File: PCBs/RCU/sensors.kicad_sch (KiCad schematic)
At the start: 4 parts

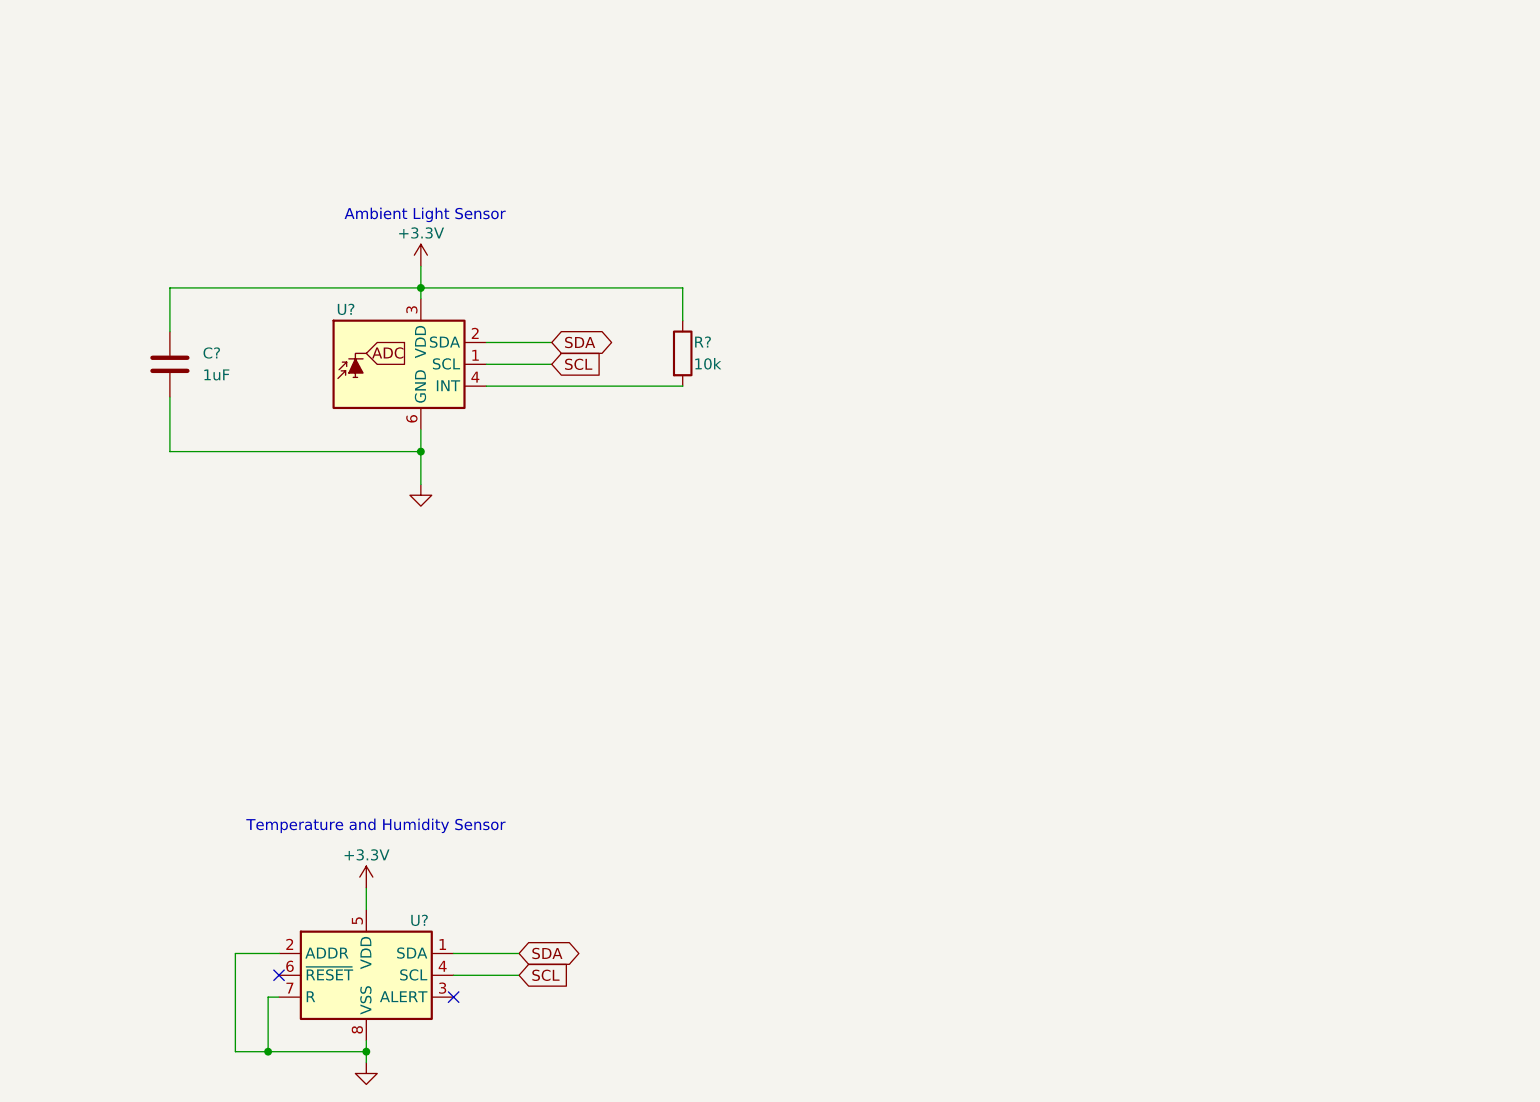
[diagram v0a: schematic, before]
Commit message: Added Accelerometer_Gyroscope IC with supplementary components
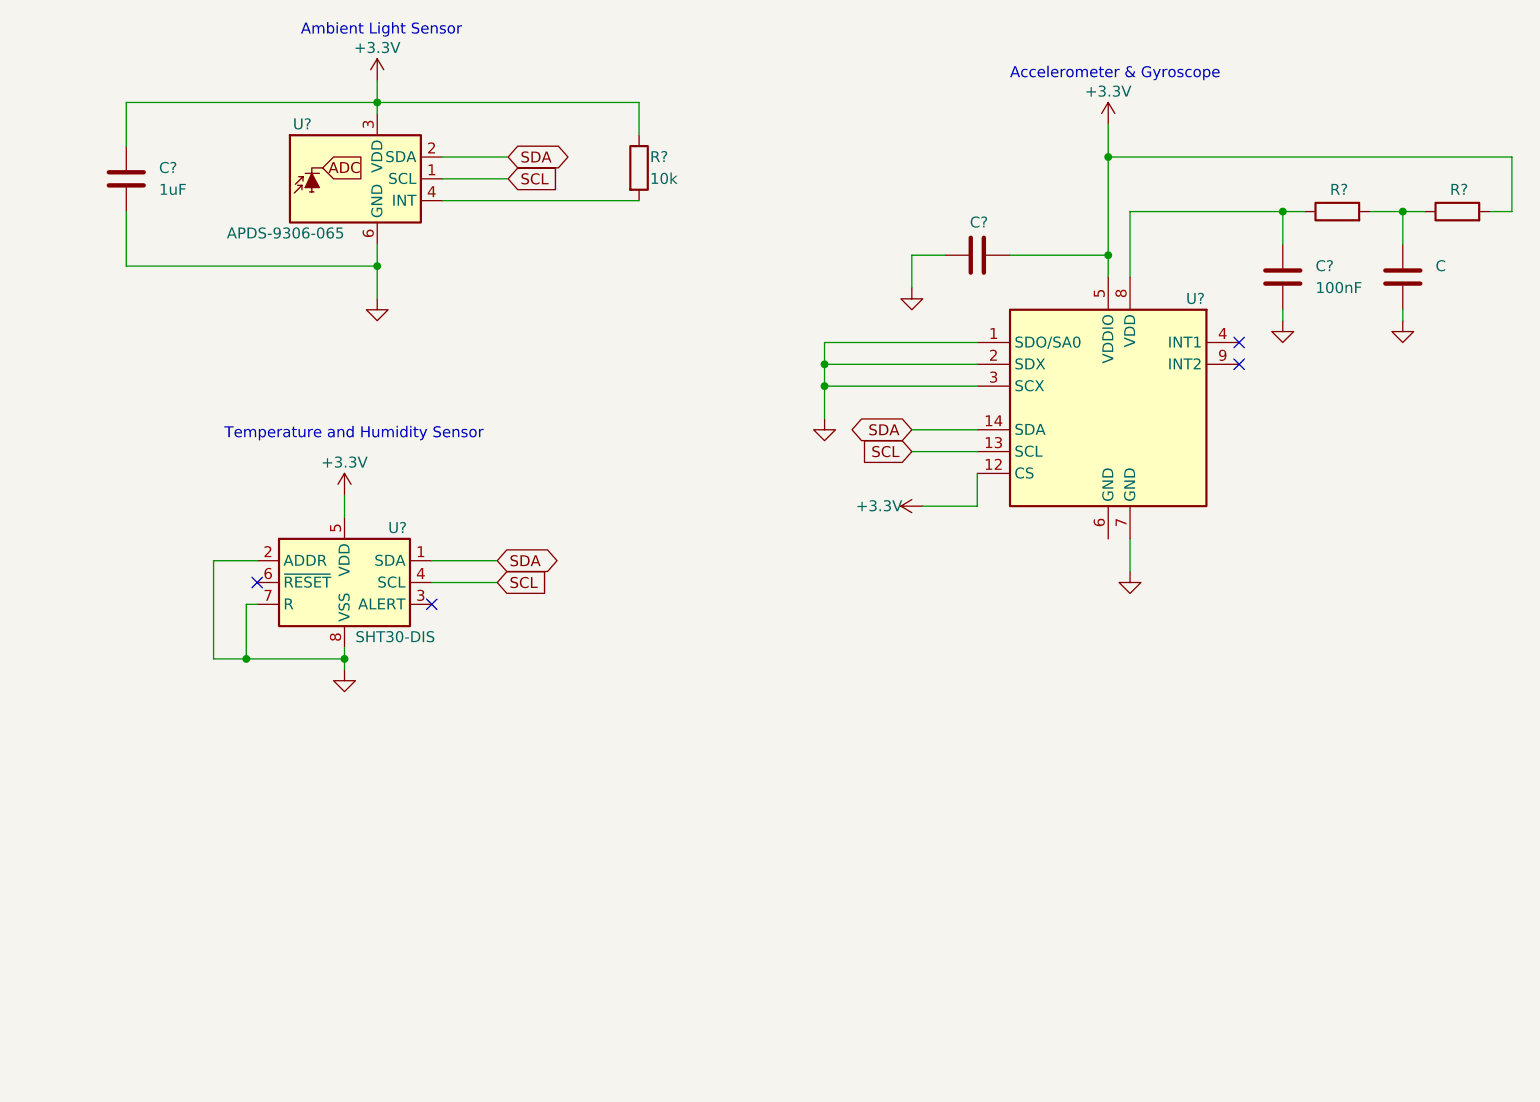
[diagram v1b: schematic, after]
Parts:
- added C, C?: (no value), symbol Device:C
- added C?: 100nF, symbol Device:C
- added R? (x2): (no value), symbol Device:R
- added U?: (no value), symbol Sensor_Motion:LSM6DS3
- U?: value (none) -> SHT30-DIS; footprint (none) -> Sensor_Humidity:Sensirion_DFN-8-1EP_2.5x2.5mm_P0.5mm_EP1.1x1.7mm
- U?: value (none) -> APDS-9306-065; footprint (none) -> OptoDevice:Broadcom_DFN-6_2x2mm_P0.65mm
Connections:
- net +3V3: now also C?.2, R?.2, U?.12 (CS), U?.5 (VDDIO)
- net GND: now also C.1, C?.1, C?.1, U?.1 (SDO/SA0), U?.2 (SDX), U?.3 (SCX), U?.7 (GND)
- net SCL: now also U?.13 (SCL)
- net SDA: now also U?.14 (SDA)
- new net: C?.2, R?.1, U?.8 (VDD)
- new net: C.2, R?.1, R?.2
- no-connect marks 2 -> 4
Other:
- note added: "Accelerometer & Gyroscope"
- moved on the sheet: C?, R?, U?

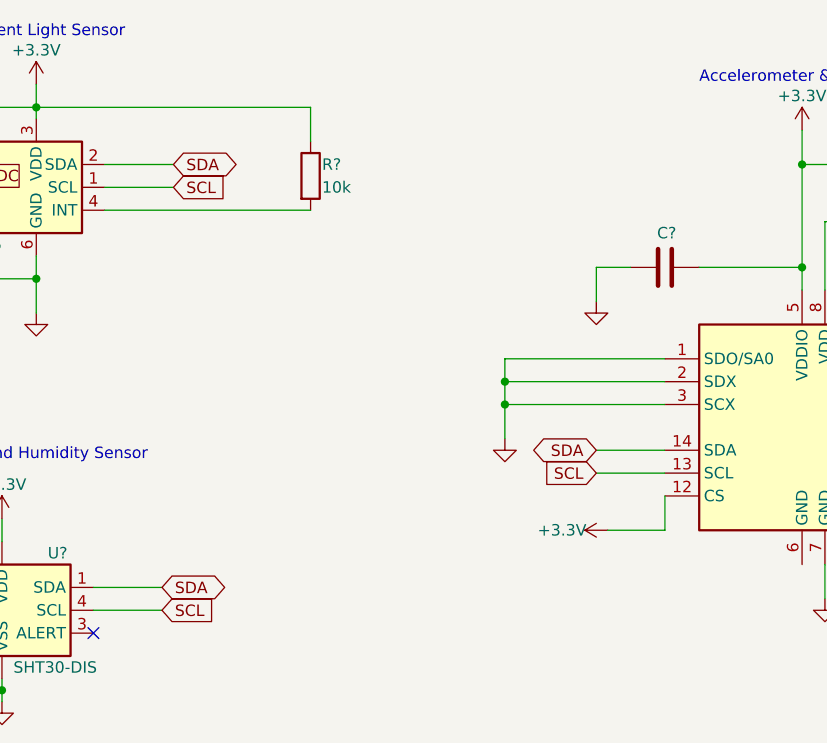
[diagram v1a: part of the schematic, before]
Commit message: Prepended 'SDA' and 'SCL' global labels with 'I2C_'
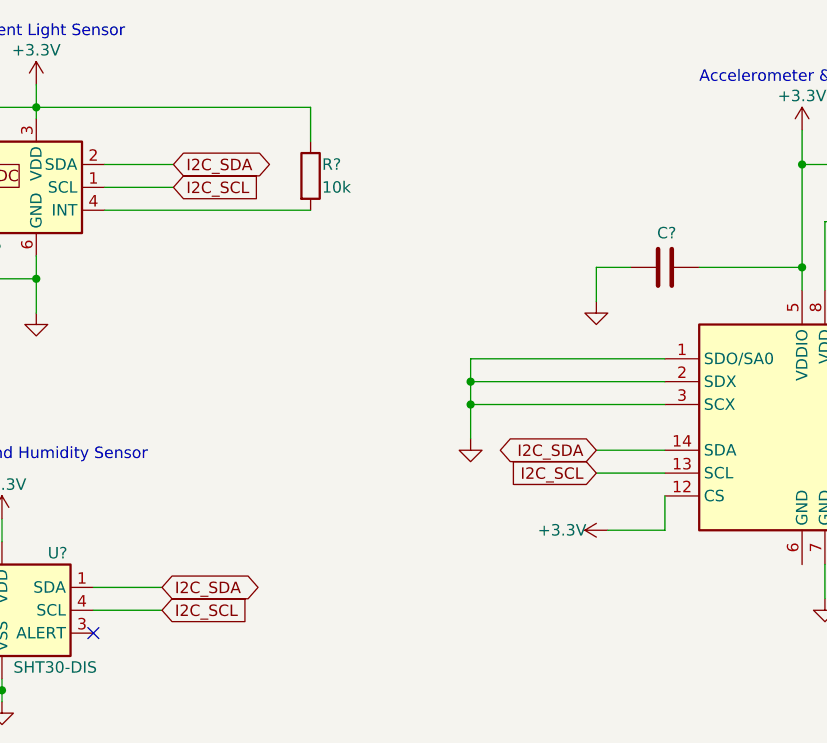
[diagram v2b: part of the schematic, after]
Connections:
- net SCL renamed I2C_SCL
- net SDA renamed I2C_SDA
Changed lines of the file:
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@@
   (junction (at 161.29 40.64) (diameter 0) (color 0 0 0 0)
   )
-  (junction (at 107.95 58.42) (diameter 0) (color 0 0 0 0)
+  (junction (at 104.14 58.42) (diameter 0) (color 0 0 0 0)
   )
   (junction (at 40.64 92.71) (diameter 0) (color 0 0 0 0)
   )
-  (junction (at 107.95 60.96) (diameter 0) (color 0 0 0 0)
+  (junction (at 104.14 60.96) (diameter 0) (color 0 0 0 0)
   )
   (no_connect (at 156.21 58.42))
@@
     (stroke (width 0) (type default) (color 0 0 0 0))
   )
+  (wire (pts (xy 104.14 58.42) (xy 125.73 58.42))
+    (stroke (width 0) (type default) (color 0 0 0 0))
+  )
   (wire (pts (xy 63.5 39.37) (xy 86.36 39.37))
     (stroke (width 0) (type default) (color 0 0 0 0))
@@
     (stroke (width 0) (type default) (color 0 0 0 0))
   )
-  (wire (pts (xy 107.95 60.96) (xy 125.73 60.96))
+  (wire (pts (xy 104.14 60.96) (xy 125.73 60.96))
     (stroke (width 0) (type default) (color 0 0 0 0))
   )
@@
     (stroke (width 0) (type default) (color 0 0 0 0))
   )
-  (wire (pts (xy 107.95 64.77) (xy 107.95 60.96))
-    (stroke (width 0) (type default) (color 0 0 0 0))
-  )
-  (wire (pts (xy 107.95 55.88) (xy 107.95 58.42))
+  (wire (pts (xy 104.14 64.77) (xy 104.14 60.96))
+    (stroke (width 0) (type default) (color 0 0 0 0))
+  )
+  (wire (pts (xy 104.14 55.88) (xy 104.14 58.42))
     (stroke (width 0) (type default) (color 0 0 0 0))
   )
@@
     (stroke (width 0) (type default) (color 0 0 0 0))
   )
-  (wire (pts (xy 107.95 58.42) (xy 107.95 60.96))
+  (wire (pts (xy 104.14 58.42) (xy 104.14 60.96))
     (stroke (width 0) (type default) (color 0 0 0 0))
   )
@@
     (stroke (width 0) (type default) (color 0 0 0 0))
   )
-  (wire (pts (xy 125.73 55.88) (xy 107.95 55.88))
+  (wire (pts (xy 104.14 55.88) (xy 125.73 55.88))
     (stroke (width 0) (type default) (color 0 0 0 0))
   )
@@
   )
   (wire (pts (xy 118.11 45.72) (xy 121.92 45.72))
-    (stroke (width 0) (type default) (color 0 0 0 0))
-  )
-  (wire (pts (xy 107.95 58.42) (xy 125.73 58.42))
     (stroke (width 0) (type default) (color 0 0 0 0))
   )
@@
     (effects (font (size 1.27 1.27)) (justify left bottom))
   )
-  (global_label "SDA" (shape bidirectional) (at 71.12 34.29 0) (fields_autoplaced)
+  (global_label "I2C_SDA" (shape bidirectional) (at 71.12 34.29 0) (fields_autoplaced)
     (effects (font (size 1.27 1.27)) (justify left))
-    (property "Intersheet References" "${INTERSHEET_REFS}" (id 0) (at 77.1012 34.2106 0)
+    (property "Intersheet References" "${INTERSHEET_REFS}" (id 0) (at 81.1531 34.2106 0)
       (effects (font (size 1.27 1.27)) (justify left) hide)
     )
   )
-  (global_label "SCL" (shape input) (at 71.12 36.83 0) (fields_autoplaced)
+  (global_label "I2C_SCL" (shape input) (at 71.12 36.83 0) (fields_autoplaced)
     (effects (font (size 1.27 1.27)) (justify left))
-    (property "Intersheet References" "${INTERSHEET_REFS}" (id 0) (at 77.0407 36.7506 0)
+    (property "Intersheet References" "${INTERSHEET_REFS}" (id 0) (at 81.0926 36.7506 0)
       (effects (font (size 1.27 1.27)) (justify left) hide)
     )
   )
-  (global_label "SDA" (shape bidirectional) (at 69.85 81.28 0) (fields_autoplaced)
+  (global_label "I2C_SDA" (shape bidirectional) (at 69.85 81.28 0) (fields_autoplaced)
     (effects (font (size 1.27 1.27)) (justify left))
-    (property "Intersheet References" "${INTERSHEET_REFS}" (id 0) (at 75.8312 81.2006 0)
+    (property "Intersheet References" "${INTERSHEET_REFS}" (id 0) (at 79.8831 81.2006 0)
       (effects (font (size 1.27 1.27)) (justify left) hide)
     )
   )
-  (global_label "SCL" (shape input) (at 118.11 68.58 180) (fields_autoplaced)
+  (global_label "I2C_SCL" (shape input) (at 118.11 68.58 180) (fields_autoplaced)
     (effects (font (size 1.27 1.27)) (justify right))
-    (property "Intersheet References" "${INTERSHEET_REFS}" (id 0) (at 112.1893 68.5006 0)
+    (property "Intersheet References" "${INTERSHEET_REFS}" (id 0) (at 108.1374 68.5006 0)
       (effects (font (size 1.27 1.27)) (justify right) hide)
     )
   )
-  (global_label "SDA" (shape bidirectional) (at 118.11 66.04 180) (fields_autoplaced)
+  (global_label "I2C_SDA" (shape bidirectional) (at 118.11 66.04 180) (fields_autoplaced)
     (effects (font (size 1.27 1.27)) (justify right))
-    (property "Intersheet References" "${INTERSHEET_REFS}" (id 0) (at 112.1288 65.9606 0)
+    (property "Intersheet References" "${INTERSHEET_REFS}" (id 0) (at 108.0769 65.9606 0)
       (effects (font (size 1.27 1.27)) (justify right) hide)
     )
   )
-  (global_label "SCL" (shape input) (at 69.85 83.82 0) (fields_autoplaced)
+  (global_label "I2C_SCL" (shape input) (at 69.85 83.82 0) (fields_autoplaced)
     (effects (font (size 1.27 1.27)) (justify left))
-    (property "Intersheet References" "${INTERSHEET_REFS}" (id 0) (at 75.7707 83.7406 0)
+    (property "Intersheet References" "${INTERSHEET_REFS}" (id 0) (at 79.8226 83.7406 0)
       (effects (font (size 1.27 1.27)) (justify left) hide)
     )
@@
     (pin "1")
   )
-  (symbol (lib_id "power:GND") (at 107.95 64.77 0) (unit 1)
-    (in_bom yes) (on_board yes) (fields_autoplaced)
-    (property "Reference" "#PWR?" (id 0) (at 107.95 71.12 0)
-      (effects (font (size 1.27 1.27)) hide)
-    )
-    (property "Value" "GND" (id 1) (at 107.95 69.85 0)
-      (effects (font (size 1.27 1.27)) hide)
-    )
-    (property "Footprint" "" (id 2) (at 107.95 64.77 0)
-      (effects (font (size 1.27 1.27)) hide)
-    )
-    (property "Datasheet" "" (id 3) (at 107.95 64.77 0)
-      (effects (font (size 1.27 1.27)) hide)
-    )
+  (symbol (lib_id "power:GND") (at 104.14 64.77 0) (unit 1)
+    (in_bom yes) (on_board yes) (fields_autoplaced)
+    (property "Reference" "#PWR?" (id 0) (at 104.14 71.12 0)
+      (effects (font (size 1.27 1.27)) hide)
+    )
+    (property "Value" "GND" (id 1) (at 104.14 69.85 0)
+      (effects (font (size 1.27 1.27)) hide)
+    )
+    (property "Footprint" "" (id 2) (at 104.14 64.77 0)
+      (effects (font (size 1.27 1.27)) hide)
+    )
+    (property "Datasheet" "" (id 3) (at 104.14 64.77 0)
+      (effects (font (size 1.27 1.27)) hide)
+    )

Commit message: Added Encoder connector terminals for left and right motors
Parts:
- C: value (none) -> 1u
- C?: value (none) -> 100nF
- R? (x2): value (none) -> 50
- U?: value (none) -> LSM6DS3; footprint (none) -> Package_LGA:LGA-14_3x2.5mm_P0.5mm_LayoutBorder3x4y
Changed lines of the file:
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@@
       (effects (font (size 1.27 1.27)) (justify left))
     )
-    (property "Value" "" (id 1) (at 168.91 43.18 90)
+    (property "Value" "50" (id 1) (at 168.91 43.18 90)
       (effects (font (size 1.27 1.27)) (justify left))
     )
@@
       (effects (font (size 1.27 1.27)) (justify right))
     )
-    (property "Value" "" (id 1) (at 179.07 49.5299 0)
+    (property "Value" "1u" (id 1) (at 179.07 49.5299 0)
       (effects (font (size 1.27 1.27)) (justify right))
     )
@@
       (effects (font (size 1.27 1.27)) (justify left))
     )
-    (property "Value" "" (id 1) (at 182.88 43.18 90)
+    (property "Value" "50" (id 1) (at 182.88 43.18 90)
       (effects (font (size 1.27 1.27)) (justify left))
     )
@@
     (in_bom yes) (on_board yes)
     (property "Reference" "U?" (id 0) (at 151.13 50.8 0))
-    (property "Value" "" (id 1) (at 148.59 76.2 0))
-    (property "Footprint" "" (id 2) (at 130.81 81.28 0)
+    (property "Value" "LSM6DS3" (id 1) (at 148.59 76.2 0))
+    (property "Footprint" "Package_LGA:LGA-14_3x2.5mm_P0.5mm_LayoutBorder3x4y" (id 2) (at 130.81 81.28 0)
       (effects (font (size 1.27 1.27)) (justify left) hide)
     )
@@
       (effects (font (size 1.27 1.27)) (justify left))
     )
-    (property "Value" "" (id 1) (at 128.27 39.37 90)
+    (property "Value" "100nF" (id 1) (at 128.27 39.37 90)
       (effects (font (size 1.27 1.27)) (justify left))
     )

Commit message: Added ADC circuit for sensing motor currents
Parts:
- C?: value 100nF -> (none)
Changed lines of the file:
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@@
       (effects (font (size 1.27 1.27)) (justify right))
     )
-    (property "Value" "100nF" (id 1) (at 165.1 49.5299 0)
+    (property "Value" "" (id 1) (at 165.1 49.5299 0)
       (effects (font (size 1.27 1.27)) (justify right))
     )

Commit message: Simulated how LPF and voltage buffer would affect current sensing reading
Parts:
- C?: value (none) -> 0.1uF
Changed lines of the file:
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@@
       (effects (font (size 1.27 1.27)) (justify right))
     )
-    (property "Value" "" (id 1) (at 165.1 49.5299 0)
+    (property "Value" "0.1uF" (id 1) (at 165.1 49.5299 0)
       (effects (font (size 1.27 1.27)) (justify right))
     )
